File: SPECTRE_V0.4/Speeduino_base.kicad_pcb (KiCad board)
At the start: 2 copper layers, 100 x 93 mm, 185 parts, among them J1 Conn_01x04_Male, J2 Conn_02x04_Odd_Even, J3 Conn_01x06_Male, Q1 2N7002, Q10 BSP78, Q11 BSP78, Q12 BSP78, Q13 BSP78, Q14 BSP78, Q15 BSP78, Q16 BSP78, Q17 BSP78, Q18 BSP78, Q2 CJ2302, Q3 CJ2302, Q4 CJ2302, Q5 BSP78, Q6 BSP78, Q7 CJ2302, Q8 CJ2302, Q9 CJ2302, U1 MAX9926UAEE+, U2 molex_48pin, U3 LM78M05_TO220, U4 MAX3232

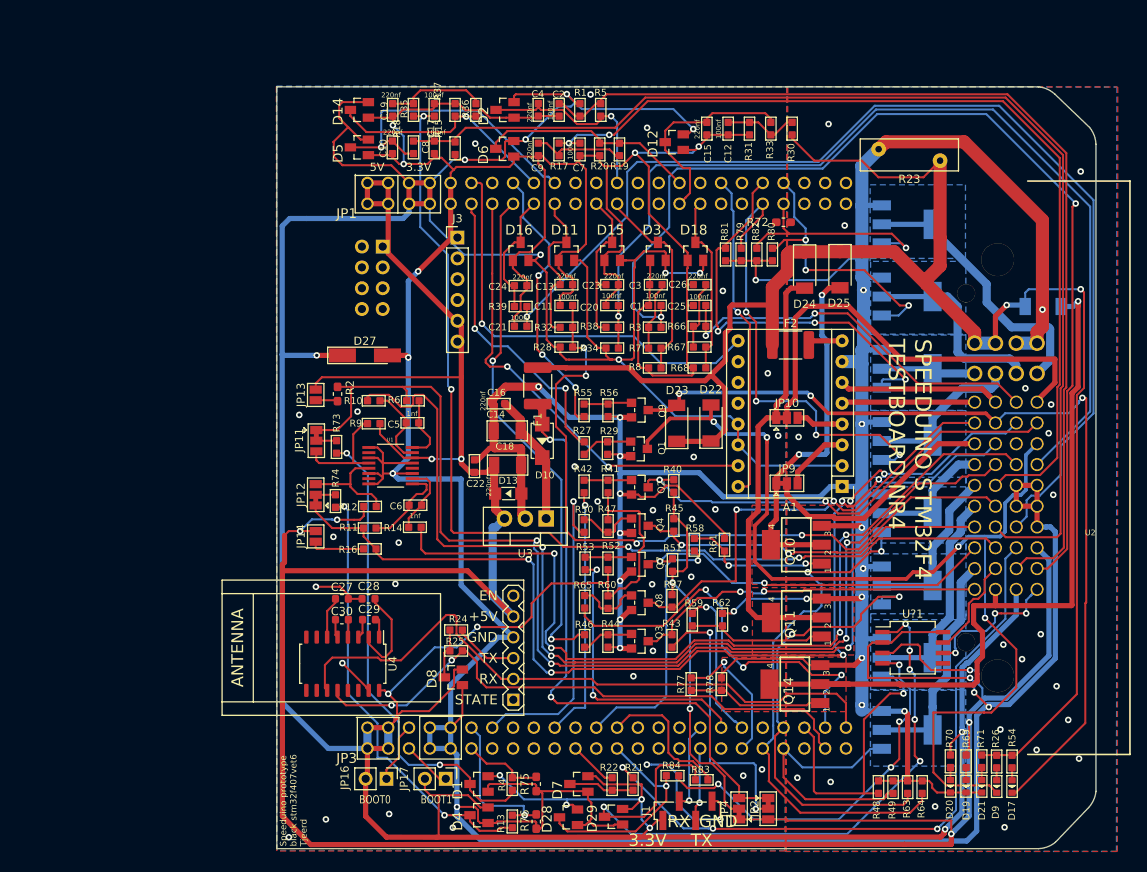
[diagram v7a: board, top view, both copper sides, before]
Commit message: rs232 + BME280 finished
Added rs232 to connector
Finished BME280 connection and routing
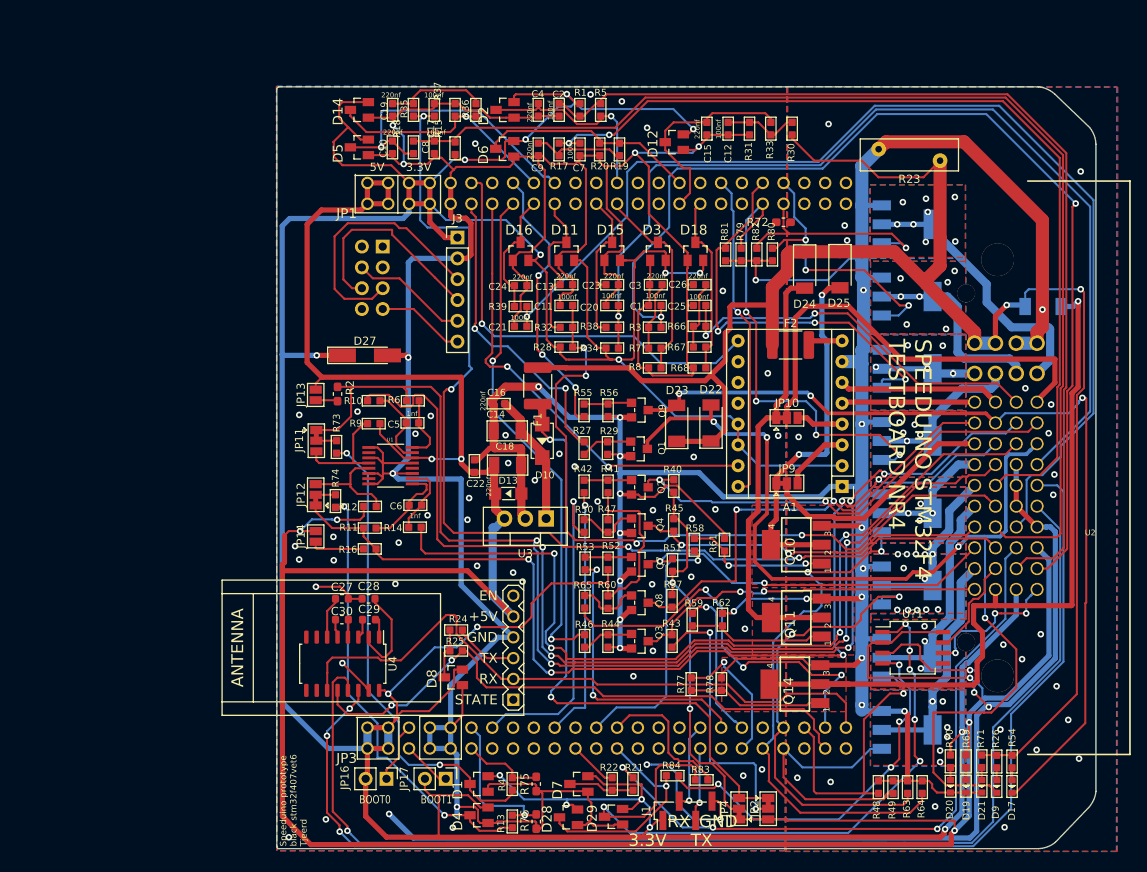
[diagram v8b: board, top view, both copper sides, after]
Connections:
- U2 pad 18: Net-(U2-Pad18) -> VR2-
- U2 pad 22: VR2- -> GND
- U2 pad 25: GND -> RS232_TX
- U2 pad 29: GND -> RS232_RX
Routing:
- net RS232_TX: track 0.00 -> 149.1 mm, vias 0 -> 3
- net RS232_RX: track 0.00 -> 145.9 mm, vias 0 -> 1
- net SPI1_SCK: track 0.00 -> 31.8 mm
- net SPI1_MOSI: track 0.00 -> 26.0 mm
- net BME280_CS: track 0.00 -> 14.4 mm
- net GND: track 565.6 -> 576.6 mm, vias 43 -> 58
- net SPI1_MISO: track 0.00 -> 10.8 mm
- net MAP: track 124.3 -> 130.4 mm
- net 3.3V: track 563.0 -> 568.1 mm
- net 5V: track 357.4 -> 360.3 mm
- net PD9: track 70.9 -> 72.3 mm
- net FUEL_PUMP: track 129.4 -> 130.1 mm
- net INJ8-OUT: vias 0 -> 8
- net PWR_GND: vias 39 -> 41
- net INJ7-OUT: vias 0 -> 7
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- added copper zone on F.Cu, net INJ1-OUT
- added copper zone on F.Cu, net INJ2-OUT
- added copper zone on F.Cu, net INJ3-OUT
- added copper zone on F.Cu, net INJ4-OUT
- added copper zone on F.Cu, net INJ5-OUT
- added copper zone on F.Cu, net INJ6-OUT
- added copper zone on F.Cu, net INJ7-OUT
- added copper zone on F.Cu, net INJ8-OUT
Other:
- outline, holes or cut-outs redrawn
